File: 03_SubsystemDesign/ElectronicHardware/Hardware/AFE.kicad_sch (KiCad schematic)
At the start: 6 parts, among them J301 RFShield_TwoPieces, U301 ISL21010C

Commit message: pcb design work in progress
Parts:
- removed U301: ISL21010C, Package_TO_SOT_SMD:SOT-23, symbol GammaSpectrometer:ISL21010C
- added U302: ISL21010CFH325Z-T7A, Package_TO_SOT_SMD:SOT-23, symbol GammaSpectrometer:ISL21010CFH325Z-T7A (2V5)
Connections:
- net AFEChannel1/1V5_REF: now also U302.2 (VOUT)
- net GND: now also U302.3 (GND)
- net +3V3_A renamed +5V0_A
- net +5V0_A: now also U302.1 (VIN)
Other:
- sheet AFEChannel1 ports: added +5V0_A; removed +3V3_A, -3V3_A
- sheet AFEChannel2 ports: added +5V0_A, 1V5_REF; removed +2V048_VREF, +5V0_AFE, -5V0_AFE

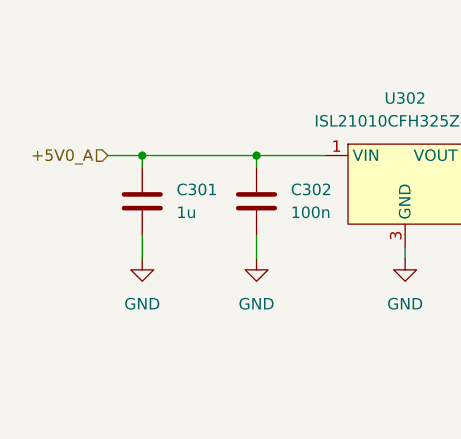
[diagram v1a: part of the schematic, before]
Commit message: improve CAD folder structure and PCB
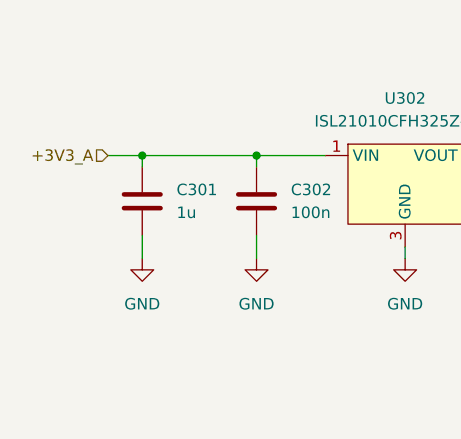
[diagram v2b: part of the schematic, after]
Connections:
- net +5V0_A: no longer C301.1, C302.1, U302.1 (VIN)
- new net +3V3_A: C301.1, C302.1, U302.1 (VIN)
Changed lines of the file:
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@@
 		)
 	)
-	(hierarchical_label "+5V0_A"
+	(hierarchical_label "+3V3_A"
 		(shape input)
 		(at 63.5 67.31 180)

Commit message: add crystal holder to pcb
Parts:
- added U301: ScintillatorCrystalHolder, GammaSpectrometer:ScintillatorCrystalHolder, symbol GammaSpectrometer:ScintillatorCrystalHolder
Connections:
- net GND: now also U301.1 (Mounting), U301.2 (Mounting), U301.3 (Mounting), U301.4 (Mounting)
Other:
- moved on the sheet: J301
